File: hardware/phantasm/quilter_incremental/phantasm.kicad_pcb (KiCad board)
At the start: 4 copper layers, 58.3 x 32 mm, 33 parts, among them J1 +5V IN ~1A, J2 LED sig DI/CI/SIG_GND, J3A SYNC in, J3B SYNC out, J4 debug, U1 74AHCT125

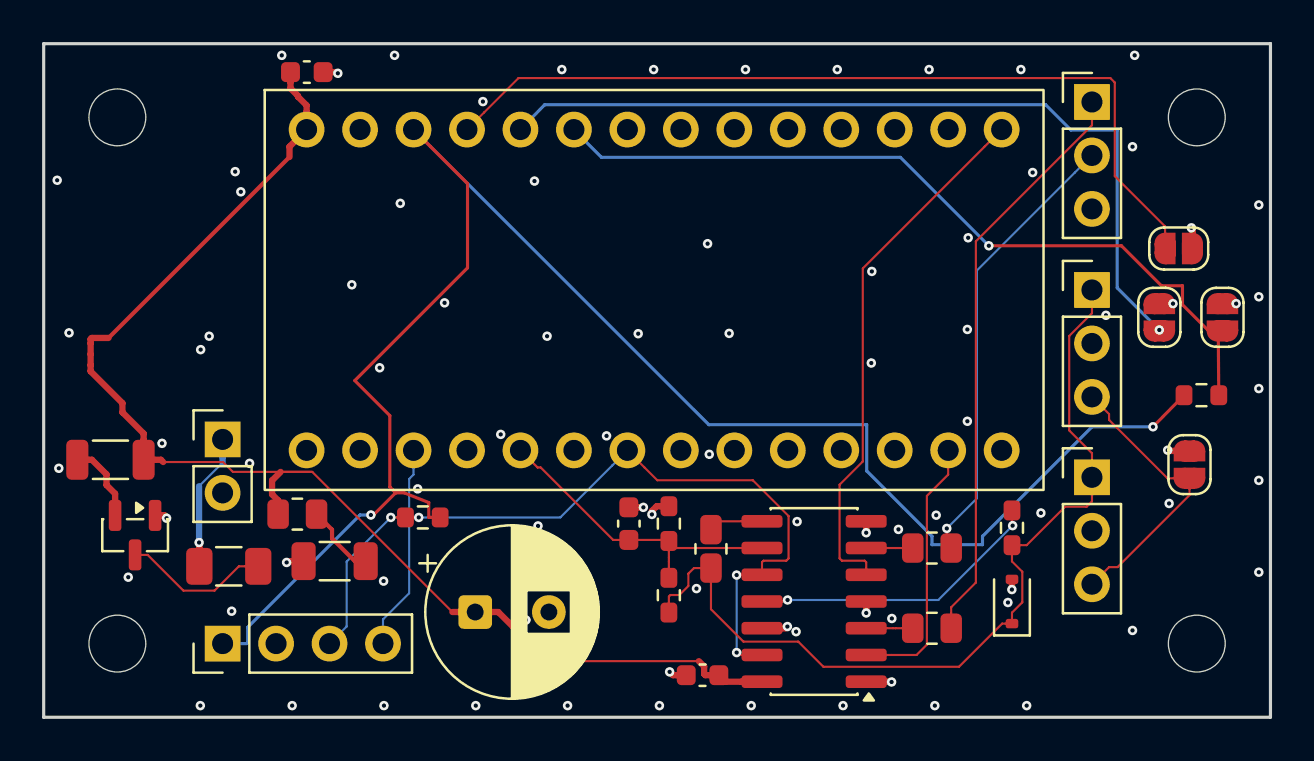
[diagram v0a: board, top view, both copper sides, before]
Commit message: phantasm: finalize routed PCB and fabrication gates
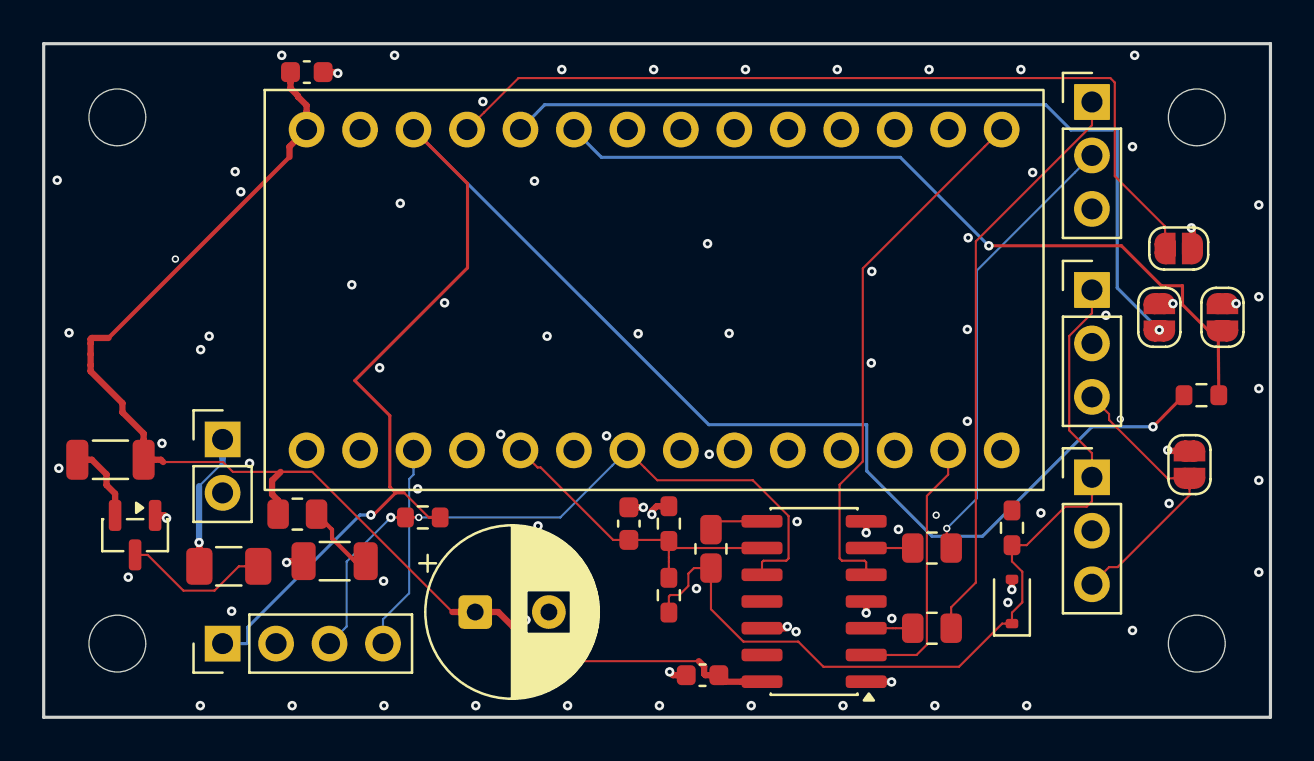
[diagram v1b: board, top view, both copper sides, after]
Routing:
- net /SYNC_PULLDOWN: track 14.1 -> 0.00 mm, vias 2 -> 0
- net /MASTER_EN: track 38.8 -> 32.7 mm, vias 4 -> 2
- net +3V3: track 85.3 -> 84.2 mm
- net GND: vias 85 -> 87
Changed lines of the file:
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@@
 		)
 		(embedded_fonts no)
-		(model "${KIPRJMOD}/phantasm.pretty/Teensy4.0.wrl"
+		(model "${KIPRJMOD}/../phantasm.pretty/Teensy4.0.wrl"
 			(offset
 				(xyz 0 0 0)
@@
 	(via
 		(at 42.4 22.4)
-		(size 0.45)
+		(size 0.35)
 		(drill 0.2)
 		(layers "F.Cu" "B.Cu")
@@
 	)
 	(via
+		(at 51.147516 17.837156)
+		(size 0.35)
+		(drill 0.2)
+		(layers "F.Cu" "B.Cu")
+		(net "GND")
+	)
+	(via
 		(at 9.096557 6.079294)
 		(size 0.45)
@@
 	)
 	(via
+		(at 6.256615 10.232849)
+		(size 0.35)
+		(drill 0.2)
+		(layers "F.Cu" "B.Cu")
+		(net "GND")
+	)
+	(via
 		(at 42.335949 31.446697)
 		(size 0.45)
@@
 	(via
 		(at 42.903329 23.029137)
-		(size 0.45)
+		(size 0.35)
 		(drill 0.2)
 		(layers "F.Cu" "B.Cu")
@@
 	)
 	(segment
-		(start 33.034474 29.04)
-		(end 33.149041 29.04)
-		(width 0.101702)
-		(layer "F.Cu")
-		(net "/MASTER_EN")
-	)
-	(segment
 		(start 28.543219 20.133219)
 		(end 28.032425 19.622425)
@@
 	)
 	(segment
-		(start 32.919762 28.925424)
-		(end 32.919898 28.92556)
-		(width 0.101702)
-		(layer "F.Cu")
-		(net "/MASTER_EN")
-	)
-	(segment
 		(start 16.78468 22.506187)
 		(end 16.490002 22.506187)
@@
 	)
 	(segment
-		(start 32.933687 25.23)
-		(end 32.919606 25.244081)
-		(width 0.101702)
-		(layer "F.Cu")
-		(net "/MASTER_EN")
-	)
-	(segment
-		(start 32.983014 25.23)
-		(end 32.933687 25.23)
-		(width 0.101702)
-		(layer "F.Cu")
-		(net "/MASTER_EN")
-	)
-	(segment
 		(start 35.386682 24.455501)
 		(end 35.386682 22.43767)
@@
 	)
 	(segment
-		(start 32.920035 28.92556)
-		(end 33.034474 29.04)
-		(width 0.101702)
-		(layer "F.Cu")
-		(net "/MASTER_EN")
-	)
-	(segment
-		(start 32.919898 28.92556)
-		(end 32.920035 28.92556)
-		(width 0.101702)
-		(layer "F.Cu")
-		(net "/MASTER_EN")
-	)
-	(segment
 		(start 17.818351 22.506)
 		(end 17.818164 22.506187)
@@
 	)
 	(segment
-		(start 33.149041 29.04)
-		(end 34.125 29.04)
-		(width 0.101702)
-		(layer "F.Cu")
-		(net "/MASTER_EN")
-	)
-	(segment
 		(start 35.386682 22.43767)
 		(end 33.688848 20.739835)
@@
 	)
 	(segment
-		(start 33.149041 25.23)
-		(end 32.983014 25.23)
-		(width 0.101702)
-		(layer "F.Cu")
-		(net "/MASTER_EN")
-	)
-	(segment
-		(start 34.125 25.23)
-		(end 33.149041 25.23)
-		(width 0.101702)
-		(layer "F.Cu")
-		(net "/MASTER_EN")
-	)
-	(segment
 		(start 35.281189 24.560994)
 		(end 35.386682 24.455501)
@@
 	)
 	(via
-		(at 32.919606 25.244081)
-		(size 0.45)
-		(drill 0.2)
-		(layers "F.Cu" "B.Cu")
-		(net "/MASTER_EN")
-	)
-	(via
 		(at 17.818351 22.506)
-		(size 0.45)
-		(drill 0.2)
-		(layers "F.Cu" "B.Cu")
-		(net "/MASTER_EN")
-	)
-	(via
-		(at 32.919762 28.925424)
-		(size 0.45)
+		(size 0.35)
 		(drill 0.2)
 		(layers "F.Cu" "B.Cu")
@@
 	)
 	(segment
-		(start 32.919762 25.244237)
-		(end 32.919762 28.925424)
-		(width 0.101702)
-		(layer "B.Cu")
-		(net "/MASTER_EN")
-	)
-	(segment
 		(start 24.544 22.506)
 		(end 17.818351 22.506)
@@
 	)
 	(segment
-		(start 32.919606 25.244081)
-		(end 32.919762 25.244237)
-		(width 0.101702)
-		(layer "B.Cu")
-		(net "/MASTER_EN")
-	)
-	(segment
-		(start 35.100959 26.5)
-		(end 35.215526 26.5)
-		(width 0.101702)
-		(layer "F.Cu")
-		(net "/SYNC_PULLDOWN")
-	)
-	(segment
-		(start 46 22.765837)
-		(end 46 22.65127)
-		(width 0.101702)
-		(layer "F.Cu")
-		(net "/SYNC_PULLDOWN")
-	)
-	(segment
-		(start 34.125 26.5)
-		(end 35.100959 26.5)
-		(width 0.101702)
-		(layer "F.Cu")
-		(net "/SYNC_PULLDOWN")
-	)
-	(segment
-		(start 35.215526 26.5)
-		(end 35.268143 26.5)
-		(width 0.101702)
-		(layer "F.Cu")
-		(net "/SYNC_PULLDOWN")
-	)
-	(segment
-		(start 35.268143 26.5)
-		(end 35.339998 26.428145)
-		(width 0.101702)
-		(layer "F.Cu")
-		(net "/SYNC_PULLDOWN")
-	)
-	(segment
-		(start 46 22.864283)
-		(end 46 22.765837)
-		(width 0.101702)
-		(layer "F.Cu")
-		(net "/SYNC_PULLDOWN")
-	)
-	(segment
-		(start 46 22.65127)
-		(end 46 22.175)
-		(width 0.101702)
-		(layer "F.Cu")
-		(net "/SYNC_PULLDOWN")
-	)
-	(segment
-		(start 46.032295 22.896578)
-		(end 46 22.864283)
-		(width 0.101702)
-		(layer "F.Cu")
-		(net "/SYNC_PULLDOWN")
-	)
-	(via
-		(at 46.032295 22.896578)
-		(size 0.45)
-		(drill 0.2)
-		(layers "F.Cu" "B.Cu")
-		(net "/SYNC_PULLDOWN")
-	)
-	(via
-		(at 35.339998 26.428145)
-		(size 0.45)
-		(drill 0.2)
-		(layers "F.Cu" "B.Cu")
-		(net "/SYNC_PULLDOWN")
-	)
-	(segment
-		(start 42.500728 26.428145)
-		(end 46.032295 22.896578)
-		(width 0.101702)
-		(layer "B.Cu")
-		(net "/SYNC_PULLDOWN")
-	)
-	(segment
-		(start 35.339998 26.428145)
-		(end 42.500728 26.428145)
-		(width 0.101702)
-		(layer "B.Cu")
-		(net "/SYNC_PULLDOWN")
-	)
-	(segment
 		(start 49.8 19.455322)
 		(end 48.720159 18.375481)
@@
 	)
 	(segment
-		(start 18.294384 21.8)
+		(start 18.294384 22.506187)
 		(end 17.124179 21.335982)
-		(width 0.15)
+		(width 0.1017)
 		(layer "F.Cu")
 		(net "+3V3")
@@
 	)
 	(segment
-		(start 18.294384 22.506187)
-		(end 18.294384 21.8)
-		(width 0.15)
-		(layer "F.Cu")
-		(net "+3V3")
-	)
-	(segment
 		(start 16.444013 17.666873)
 		(end 14.781011 16.003871)
@@
 	)
 	(segment
-		(start 44.6 23.8)
-		(end 44.6 23.4)
-		(width 0.15)
-		(layer "B.Cu")
-		(net "+3V3")
-	)
-	(segment
 		(start 49.8 18.2)
 		(end 52.7 18.2)
@@
 	)
 	(segment
-		(start 42.2 23.4)
-		(end 42.2 23.8)
+		(start 9.35 28.5)
+		(end 9.644678 28.5)
 		(width 0.15)
 		(layer "B.Cu")
@@
 	)
 	(segment
-		(start 9.35 28.5)
-		(end 9.644678 28.5)
+		(start 42.2 23.4)
+		(end 44.6 23.4)
 		(width 0.15)
 		(layer "B.Cu")
@@
 		(width 0.15)
 		(layer "B.Cu")
-		(net "+3V3")
-	)
-	(segment
-		(start 42.2 23.8)
-		(end 44.6 23.8)
-		(width 0.15)
-		(layer "B.Cu")
